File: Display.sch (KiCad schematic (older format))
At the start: 16 parts, among them Q1 Q_NPN_BCE, Q2 Q_NPN_BCE, U1 74LS47, U5 DA56-11GWA

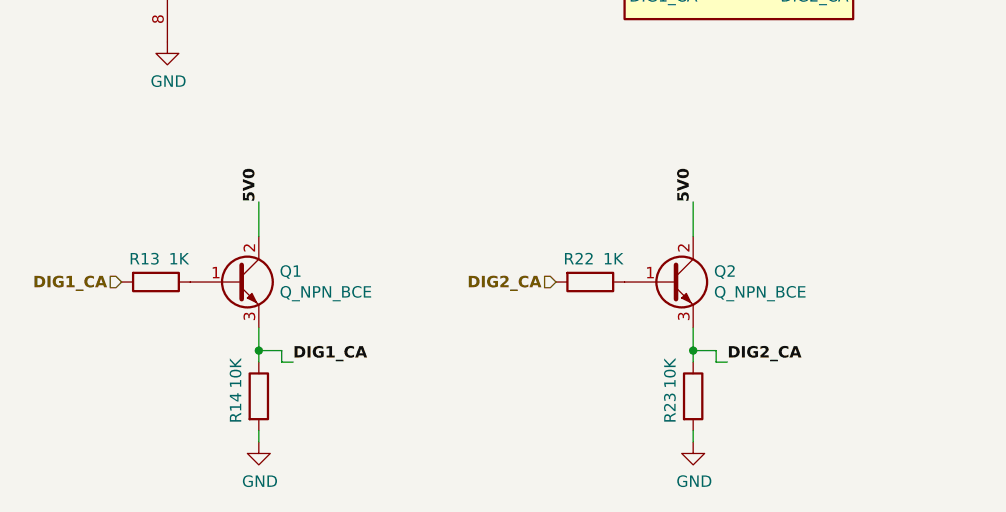
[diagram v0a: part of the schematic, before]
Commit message: Se agrega bus a jerarquia y pines de programación icsp
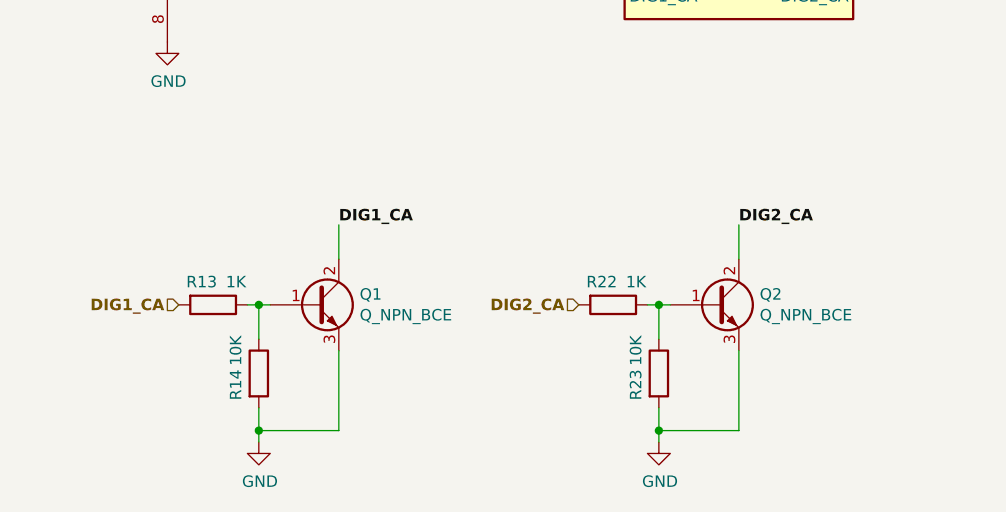
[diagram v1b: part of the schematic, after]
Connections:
- wire segments 26 -> 28
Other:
- moved on the sheet: Q2, R22, R23
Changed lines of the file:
@@
 EESchema Schematic File Version 4
+LIBS:TPDSI_1-cache
 EELAYER 29 0
 EELAYER END
@@
 Sheet 5 5
 Title "Kit Development for MCU PIC"
-Date "2019-05-05"
-Rev "1.0"
+Date "2019-05-06"
+Rev "1.1"
 Comp "Julian Bustamante Narvaez"
 Comment1 ""
@@
 	1    0    0    -1
 $EndComp
-$Comp
-L Device:Q_NPN_BCE Q1
-U 1 1 5CDF134E
-P 4250 4700
-F 0 "Q1" H 4441 4746 50  0000 L CNN
-F 1 "Q_NPN_BCE" H 4441 4655 50  0000 L CNN
-F 2 "" H 4450 4800 50  0001 C CNN
-F 3 "~" H 4250 4700 50  0001 C CNN
-	1    4250 4700
-	1    0    0    -1
-$EndComp
-$Comp
-L Device:R R13
-U 1 1 5CDF2A90
-P 3900 4700
-F 0 "R13" V 3800 4650 50  0000 C CNN
-F 1 "1K" V 3800 4800 50  0000 C CNN
-F 2 "" V 3830 4700 50  0001 C CNN
-F 3 "~" H 3900 4700 50  0001 C CNN
-	1    3900 4700
-	0    1    1    0
-$EndComp
 Wire Wire Line
 	7050 3450 7150 3450
 Text Label 7150 3450 0    50   ~ 10
 DIG2_CA
-Text Label 4500 5050 0    50   ~ 10
+Text Label 4700 4450 0    50   ~ 10
 DIG1_CA
-$Comp
-L Device:R R14
-U 1 1 5CDF7698
-P 4350 5200
-F 0 "R14" V 4250 5150 50  0000 C CNN
-F 1 "10K" V 4250 5300 50  0000 C CNN
-F 2 "" V 4280 5200 50  0001 C CNN
-F 3 "~" H 4350 5200 50  0001 C CNN
-	1    4350 5200
-	1    0    0    -1
-$EndComp
-$Comp
-L power:GND #PWR020
-U 1 1 5CDF8A2B
-P 4350 5400
-F 0 "#PWR020" H 4350 5150 50  0001 C CNN
-F 1 "GND" H 4355 5227 50  0000 C CNN
-F 2 "" H 4350 5400 50  0001 C CNN
-F 3 "" H 4350 5400 50  0001 C CNN
-	1    4350 5400
-	1    0    0    -1
-$EndComp
-Wire Wire Line
-	4350 4900 4350 5000
-Wire Wire Line
-	4500 5050 4450 5050
-Wire Wire Line
-	4450 5050 4450 5000
-Wire Wire Line
-	4450 5000 4350 5000
-Connection ~ 4350 5000
-Wire Wire Line
-	4350 5000 4350 5050
-Wire Wire Line
-	4350 5400 4350 5350
-Text Label 4350 4350 1    50   ~ 10
-5V0
-Wire Wire Line
-	4350 4350 4350 4500
 Text GLabel 5250 1800 0    50   Output ~ 10
 +5V0
@@
 L Device:Q_NPN_BCE Q2
 U 1 1 5CDFE125
-P 6150 4700
-F 0 "Q2" H 6341 4746 50  0000 L CNN
-F 1 "Q_NPN_BCE" H 6341 4655 50  0000 L CNN
-F 2 "" H 6350 4800 50  0001 C CNN
-F 3 "~" H 6150 4700 50  0001 C CNN
-	1    6150 4700
+P 6350 4800
+F 0 "Q2" H 6541 4846 50  0000 L CNN
+F 1 "Q_NPN_BCE" H 6541 4755 50  0000 L CNN
+F 2 "" H 6550 4900 50  0001 C CNN
+F 3 "~" H 6350 4800 50  0001 C CNN
+	1    6350 4800
 	1    0    0    -1
 $EndComp
@@
 L Device:R R22
 U 1 1 5CDFE12F
-P 5800 4700
-F 0 "R22" V 5700 4650 50  0000 C CNN
-F 1 "1K" V 5700 4800 50  0000 C CNN
-F 2 "" V 5730 4700 50  0001 C CNN
-F 3 "~" H 5800 4700 50  0001 C CNN
-	1    5800 4700
-	0    1    1    0
-$EndComp
-Text Label 6400 5050 0    50   ~ 10
+P 5900 4800
+F 0 "R22" V 5800 4750 50  0000 C CNN
+F 1 "1K" V 5800 4900 50  0000 C CNN
+F 2 "" V 5830 4800 50  0001 C CNN
+F 3 "~" H 5900 4800 50  0001 C CNN
+	1    5900 4800
+	0    1    1    0
+$EndComp
+Text Label 6450 4450 0    50   ~ 10
 DIG2_CA
-$Comp
-L Device:R R23
-U 1 1 5CDFE13A
-P 6250 5200
-F 0 "R23" V 6150 5150 50  0000 C CNN
-F 1 "10K" V 6150 5300 50  0000 C CNN
-F 2 "" V 6180 5200 50  0001 C CNN
-F 3 "~" H 6250 5200 50  0001 C CNN
-	1    6250 5200
-	1    0    0    -1
-$EndComp
 $Comp
 L power:GND #PWR022
 U 1 1 5CDFE144
-P 6250 5400
-F 0 "#PWR022" H 6250 5150 50  0001 C CNN
-F 1 "GND" H 6255 5227 50  0000 C CNN
-F 2 "" H 6250 5400 50  0001 C CNN
-F 3 "" H 6250 5400 50  0001 C CNN
-	1    6250 5400
-	1    0    0    -1
-$EndComp
-Wire Wire Line
-	6250 4900 6250 5000
-Wire Wire Line
-	6400 5050 6350 5050
-Wire Wire Line
-	6350 5050 6350 5000
-Wire Wire Line
-	6350 5000 6250 5000
-Connection ~ 6250 5000
-Wire Wire Line
-	6250 5000 6250 5050
-Wire Wire Line
-	6250 5400 6250 5350
-Text Label 6250 4350 1    50   ~ 10
-5V0
-Wire Wire Line
-	6250 4350 6250 4500
+P 6100 5400
+F 0 "#PWR022" H 6100 5150 50  0001 C CNN
+F 1 "GND" H 6105 5227 50  0000 C CNN
+F 2 "" H 6100 5400 50  0001 C CNN
+F 3 "" H 6100 5400 50  0001 C CNN
+	1    6100 5400
+	1    0    0    -1
+$EndComp
 Text Label 5800 3450 2    50   ~ 10
 DIG1_CA
@@
 Text HLabel 3450 2950 0    50   Input ~ 10
 D
-Text HLabel 5650 4700 0    50   Input ~ 10
+Text HLabel 5750 4800 0    50   Input ~ 10
 DIG2_CA
-Text HLabel 3750 4700 0    50   Input ~ 10
+Text HLabel 4000 4800 0    50   Input ~ 10
 DIG1_CA
 Text HLabel 5850 3350 0    50   Input ~ 10
@@
 Wire Wire Line
 	4100 2350 3950 2350
+Wire Wire Line
+	6450 4450 6450 4600
+$Comp
+L Device:R R23
+U 1 1 5CDFE13A
+P 6100 5100
+F 0 "R23" V 6000 5050 50  0000 C CNN
+F 1 "10K" V 6000 5200 50  0000 C CNN
+F 2 "" V 6030 5100 50  0001 C CNN
+F 3 "~" H 6100 5100 50  0001 C CNN
+	1    6100 5100
+	1    0    0    -1
+$EndComp
+Wire Wire Line
+	6050 4800 6100 4800
+Wire Wire Line
+	6100 4950 6100 4800
+Connection ~ 6100 4800
+Wire Wire Line
+	6100 4800 6150 4800
+Wire Wire Line
+	6100 5250 6100 5350
+Wire Wire Line
+	6450 5350 6100 5350
+Connection ~ 6100 5350
+Wire Wire Line
+	6100 5350 6100 5400
+Wire Wire Line
+	6450 5000 6450 5350
+$Comp
+L Device:Q_NPN_BCE Q1
+U 1 1 5CD2B4DB
+P 4600 4800
+F 0 "Q1" H 4791 4846 50  0000 L CNN
+F 1 "Q_NPN_BCE" H 4791 4755 50  0000 L CNN
+F 2 "" H 4800 4900 50  0001 C CNN
+F 3 "~" H 4600 4800 50  0001 C CNN
+	1    4600 4800
+	1    0    0    -1
+$EndComp
+$Comp
+L Device:R R13
+U 1 1 5CD2B4E5
+P 4150 4800
+F 0 "R13" V 4050 4750 50  0000 C CNN
+F 1 "1K" V 4050 4900 50  0000 C CNN
+F 2 "" V 4080 4800 50  0001 C CNN
+F 3 "~" H 4150 4800 50  0001 C CNN
+	1    4150 4800
+	0    1    1    0
+$EndComp
+$Comp
+L power:GND #PWR020
+U 1 1 5CD2B4F0
+P 4350 5400
+F 0 "#PWR020" H 4350 5150 50  0001 C CNN
+F 1 "GND" H 4355 5227 50  0000 C CNN
+F 2 "" H 4350 5400 50  0001 C CNN
+F 3 "" H 4350 5400 50  0001 C CNN
+	1    4350 5400
+	1    0    0    -1
+$EndComp
+Wire Wire Line
+	4700 4450 4700 4600
+$Comp
+L Device:R R14
+U 1 1 5CD2B4FC
+P 4350 5100
+F 0 "R14" V 4250 5050 50  0000 C CNN
+F 1 "10K" V 4250 5200 50  0000 C CNN
+F 2 "" V 4280 5100 50  0001 C CNN
+F 3 "~" H 4350 5100 50  0001 C CNN
+	1    4350 5100
+	1    0    0    -1
+$EndComp
+Wire Wire Line
+	4300 4800 4350 4800
+Wire Wire Line
+	4350 4950 4350 4800
+Connection ~ 4350 4800
+Wire Wire Line
+	4350 4800 4400 4800
+Wire Wire Line
+	4350 5250 4350 5350
+Wire Wire Line
+	4700 5350 4350 5350
+Connection ~ 4350 5350
+Wire Wire Line
+	4350 5350 4350 5400
+Wire Wire Line
+	4700 5000 4700 5350
 $EndSCHEMATC

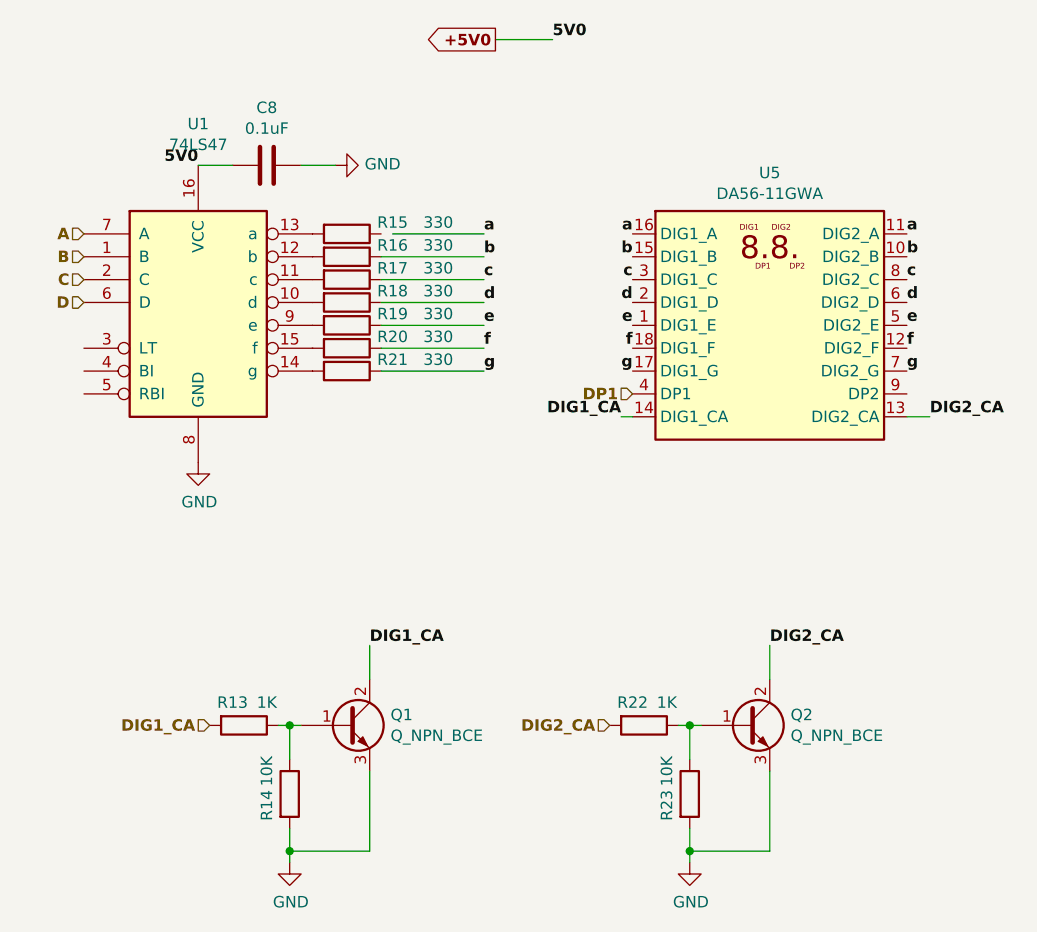
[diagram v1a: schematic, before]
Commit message: Se Organiza conexiones de alimentacion con elementos de la biblioteca power, se quitan algunas etiquetas y se coloca la fuente en hoja principal
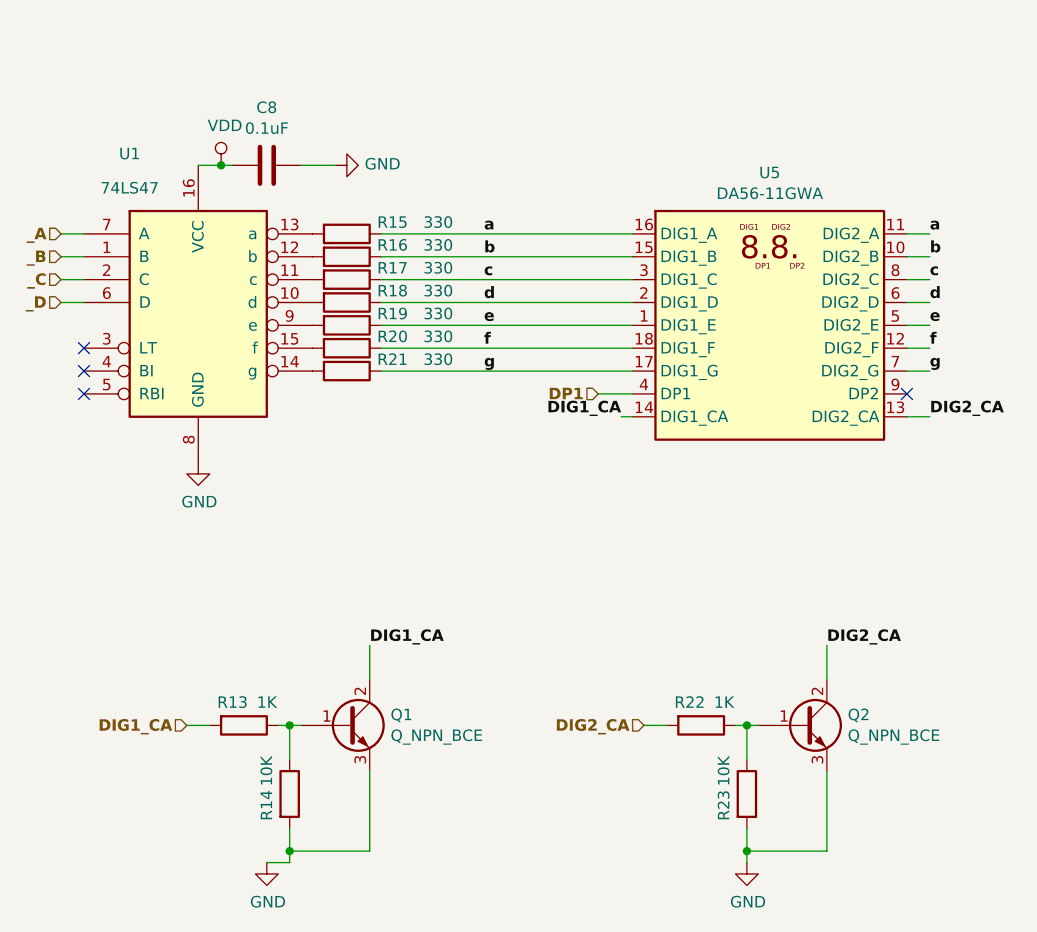
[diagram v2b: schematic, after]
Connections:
- net labels added: VDD, _A, _B, _C, _D
- net labels removed: +5V0, 5V0, A, B, C, D
- wire segments 28 -> 43
- no-connect marks 0 -> 4
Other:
- moved on the sheet: Q2, R22, R23
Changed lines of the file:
@@
 $Descr A4 11693 8268
 encoding utf-8
-Sheet 5 5
+Sheet 4 4
 Title "Kit Development for MCU PIC"
-Date "2019-05-06"
-Rev "1.1"
+Date "2019-05-14"
+Rev "1.2"
 Comp "Julian Bustamante Narvaez"
 Comment1 ""
@@
 U 1 1 5CDD9840
 P 3950 2950
-F 0 "U1" H 3950 3731 50  0000 C CNN
-F 1 "74LS47" H 3950 3640 50  0000 C CNN
+F 0 "U1" H 3650 3600 50  0000 C CNN
+F 1 "74LS47" H 3650 3450 50  0000 C CNN
 F 2 "" H 3950 2950 50  0001 C CNN
 F 3 "http://www.ti.com/lit/gpn/sn74LS47" H 3950 2950 50  0001 C CNN
@@
 Text Label 5200 3250 0    50   ~ 10
 g
-Text Label 5850 3250 2    50   ~ 10
+Text Label 7150 3250 0    50   ~ 10
 g
-Text Label 5850 3150 2    50   ~ 10
+Text Label 7150 3150 0    50   ~ 10
 f
-Text Label 5850 3050 2    50   ~ 10
+Text Label 7150 3050 0    50   ~ 10
 e
-Text Label 5850 2950 2    50   ~ 10
+Text Label 7150 2950 0    50   ~ 10
 d
-Text Label 5850 2850 2    50   ~ 10
+Text Label 7150 2850 0    50   ~ 10
 c
-Text Label 5850 2750 2    50   ~ 10
+Text Label 7150 2750 0    50   ~ 10
 b
-Text Label 5850 2650 2    50   ~ 10
-a
-Text Label 7050 3250 0    50   ~ 10
-g
-Text Label 7050 3150 0    50   ~ 10
-f
-Text Label 7050 3050 0    50   ~ 10
-e
-Text Label 7050 2950 0    50   ~ 10
-d
-Text Label 7050 2850 0    50   ~ 10
-c
-Text Label 7050 2750 0    50   ~ 10
-b
-Text Label 7050 2650 0    50   ~ 10
+Text Label 7150 2650 0    50   ~ 10
 a
 Wire Wire Line
@@
 	0    1    1    0
 $EndComp
-Wire Wire Line
-	4800 2650 5200 2650
-Wire Wire Line
-	4750 2750 5200 2750
-Wire Wire Line
-	4750 2850 5200 2850
-Wire Wire Line
-	4750 2950 5200 2950
-Wire Wire Line
-	4750 3050 5200 3050
-Wire Wire Line
-	4750 3150 5200 3150
-Wire Wire Line
-	4750 3250 5200 3250
-Text Label 5500 1800 0    50   ~ 10
-5V0
-Text Label 3950 2350 2    50   ~ 10
-5V0
 $Comp
 L power:GND #PWR019
@@
 Text Label 4700 4450 0    50   ~ 10
 DIG1_CA
-Text GLabel 5250 1800 0    50   Output ~ 10
-+5V0
-Wire Wire Line
-	5500 1800 5250 1800
 $Comp
 L Device:Q_NPN_BCE Q2
 U 1 1 5CDFE125
-P 6350 4800
-F 0 "Q2" H 6541 4846 50  0000 L CNN
-F 1 "Q_NPN_BCE" H 6541 4755 50  0000 L CNN
-F 2 "" H 6550 4900 50  0001 C CNN
-F 3 "~" H 6350 4800 50  0001 C CNN
-	1    6350 4800
+P 6600 4800
+F 0 "Q2" H 6791 4846 50  0000 L CNN
+F 1 "Q_NPN_BCE" H 6791 4755 50  0000 L CNN
+F 2 "" H 6800 4900 50  0001 C CNN
+F 3 "~" H 6600 4800 50  0001 C CNN
+	1    6600 4800
 	1    0    0    -1
 $EndComp
@@
 L Device:R R22
 U 1 1 5CDFE12F
-P 5900 4800
-F 0 "R22" V 5800 4750 50  0000 C CNN
-F 1 "1K" V 5800 4900 50  0000 C CNN
-F 2 "" V 5830 4800 50  0001 C CNN
-F 3 "~" H 5900 4800 50  0001 C CNN
-	1    5900 4800
-	0    1    1    0
-$EndComp
-Text Label 6450 4450 0    50   ~ 10
+P 6150 4800
+F 0 "R22" V 6050 4750 50  0000 C CNN
+F 1 "1K" V 6050 4900 50  0000 C CNN
+F 2 "" V 6080 4800 50  0001 C CNN
+F 3 "~" H 6150 4800 50  0001 C CNN
+	1    6150 4800
+	0    1    1    0
+$EndComp
+Text Label 6700 4450 0    50   ~ 10
 DIG2_CA
 $Comp
 L power:GND #PWR022
 U 1 1 5CDFE144
-P 6100 5400
-F 0 "#PWR022" H 6100 5150 50  0001 C CNN
-F 1 "GND" H 6105 5227 50  0000 C CNN
-F 2 "" H 6100 5400 50  0001 C CNN
-F 3 "" H 6100 5400 50  0001 C CNN
-	1    6100 5400
+P 6350 5400
+F 0 "#PWR022" H 6350 5150 50  0001 C CNN
+F 1 "GND" H 6355 5227 50  0000 C CNN
+F 2 "" H 6350 5400 50  0001 C CNN
+F 3 "" H 6350 5400 50  0001 C CNN
+	1    6350 5400
 	1    0    0    -1
 $EndComp
 Text Label 5800 3450 2    50   ~ 10
 DIG1_CA
-Text HLabel 3450 2650 0    50   Input ~ 10
-A
-Text HLabel 3450 2750 0    50   Input ~ 10
-B
-Text HLabel 3450 2850 0    50   Input ~ 10
-C
-Text HLabel 3450 2950 0    50   Input ~ 10
-D
-Text HLabel 5750 4800 0    50   Input ~ 10
+Text HLabel 3350 2650 0    50   Input ~ 10
+_A
+Text HLabel 3350 2750 0    50   Input ~ 10
+_B
+Text HLabel 3350 2850 0    50   Input ~ 10
+_C
+Text HLabel 3350 2950 0    50   Input ~ 10
+_D
+Text HLabel 5900 4800 0    50   Input ~ 10
 DIG2_CA
-Text HLabel 4000 4800 0    50   Input ~ 10
+Text HLabel 3900 4800 0    50   Input ~ 10
 DIG1_CA
-Text HLabel 5850 3350 0    50   Input ~ 10
+Text HLabel 5700 3350 0    50   Input ~ 10
 DP1
 $Comp
@@
 $EndComp
 Wire Wire Line
-	4100 2350 3950 2350
-Wire Wire Line
-	6450 4450 6450 4600
+	6700 4450 6700 4600
 $Comp
 L Device:R R23
 U 1 1 5CDFE13A
-P 6100 5100
-F 0 "R23" V 6000 5050 50  0000 C CNN
-F 1 "10K" V 6000 5200 50  0000 C CNN
-F 2 "" V 6030 5100 50  0001 C CNN
-F 3 "~" H 6100 5100 50  0001 C CNN
-	1    6100 5100
-	1    0    0    -1
-$EndComp
-Wire Wire Line
-	6050 4800 6100 4800
-Wire Wire Line
-	6100 4950 6100 4800
-Connection ~ 6100 4800
-Wire Wire Line
-	6100 4800 6150 4800
-Wire Wire Line
-	6100 5250 6100 5350
-Wire Wire Line
-	6450 5350 6100 5350
-Connection ~ 6100 5350
-Wire Wire Line
-	6100 5350 6100 5400
-Wire Wire Line
-	6450 5000 6450 5350
+P 6350 5100
+F 0 "R23" V 6250 5050 50  0000 C CNN
+F 1 "10K" V 6250 5200 50  0000 C CNN
+F 2 "" V 6280 5100 50  0001 C CNN
+F 3 "~" H 6350 5100 50  0001 C CNN
+	1    6350 5100
+	1    0    0    -1
+$EndComp
+Wire Wire Line
+	6300 4800 6350 4800
+Wire Wire Line
+	6350 4950 6350 4800
+Connection ~ 6350 4800
+Wire Wire Line
+	6350 4800 6400 4800
+Wire Wire Line
+	6350 5250 6350 5350
+Wire Wire Line
+	6700 5350 6350 5350
+Connection ~ 6350 5350
+Wire Wire Line
+	6350 5350 6350 5400
+Wire Wire Line
+	6700 5000 6700 5350
 $Comp
 L Device:Q_NPN_BCE Q1
@@
 L power:GND #PWR020
 U 1 1 5CD2B4F0
-P 4350 5400
-F 0 "#PWR020" H 4350 5150 50  0001 C CNN
-F 1 "GND" H 4355 5227 50  0000 C CNN
-F 2 "" H 4350 5400 50  0001 C CNN
-F 3 "" H 4350 5400 50  0001 C CNN
-	1    4350 5400
+P 4250 5400
+F 0 "#PWR020" H 4250 5150 50  0001 C CNN
+F 1 "GND" H 4255 5227 50  0000 C CNN
+F 2 "" H 4250 5400 50  0001 C CNN
+F 3 "" H 4250 5400 50  0001 C CNN
+	1    4250 5400
 	1    0    0    -1
 $EndComp
@@
 Wire Wire Line
 	4700 5000 4700 5350
+NoConn ~ 3450 3150
+NoConn ~ 3450 3250
+NoConn ~ 3450 3350
+NoConn ~ 7050 3350
+Wire Wire Line
+	4750 3250 5850 3250
+Wire Wire Line
+	4750 3150 5850 3150
+Wire Wire Line
+	4750 3050 5850 3050
+Wire Wire Line
+	4750 2950 5850 2950
+Wire Wire Line
+	4750 2850 5850 2850
+Wire Wire Line
+	4750 2750 5850 2750
+Wire Wire Line
+	4750 2650 5850 2650
+Wire Wire Line
+	7050 2650 7150 2650
+Wire Wire Line
+	7050 2750 7150 2750
+Wire Wire Line
+	7050 2850 7150 2850
+Wire Wire Line
+	7050 2950 7150 2950
+Wire Wire Line
+	7050 3050 7150 3050
+Wire Wire Line
+	7050 3150 7150 3150
+Wire Wire Line
+	7050 3250 7150 3250
+Wire Wire Line
+	5850 3350 5700 3350
+Wire Wire Line
+	3900 4800 4000 4800
+Wire Wire Line
+	6000 4800 5900 4800
+$Comp
+L power:VDD #PWR0120
+U 1 1 5CF6D9AF
+P 4050 2350
+F 0 "#PWR0120" H 4050 2200 50  0001 C CNN
+F 1 "VDD" H 4067 2523 50  0000 C CNN
+F 2 "" H 4050 2350 50  0001 C CNN
+F 3 "" H 4050 2350 50  0001 C CNN
+	1    4050 2350
+	1    0    0    -1
+$EndComp
+Wire Wire Line
+	3450 2650 3350 2650
+Wire Wire Line
+	3450 2750 3350 2750
+Wire Wire Line
+	3450 2850 3350 2850
+Wire Wire Line
+	3450 2950 3350 2950
+Wire Wire Line
+	4350 5400 4250 5400
+Wire Wire Line
+	3950 2350 4050 2350
+Wire Wire Line
+	4050 2350 4100 2350
+Connection ~ 4050 2350
 $EndSCHEMATC
